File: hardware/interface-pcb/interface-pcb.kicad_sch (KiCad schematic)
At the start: 0 parts

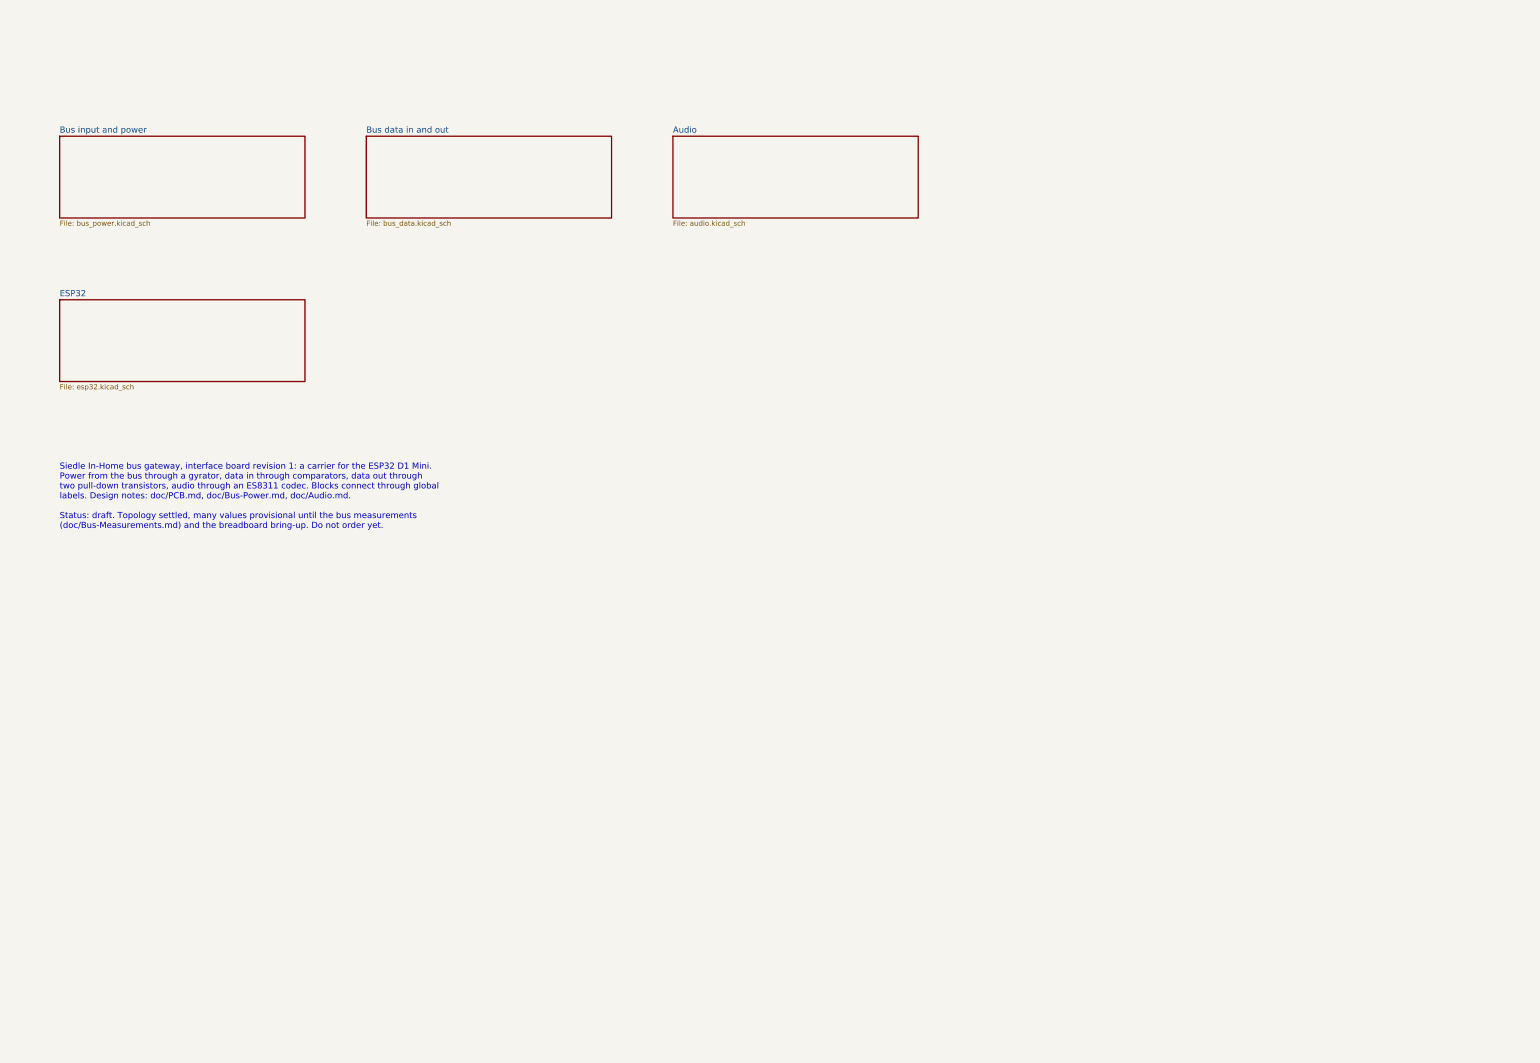
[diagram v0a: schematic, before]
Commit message: Redraw the schematic with wires
The generated draft connected everything through net labels. The redraw
wires each block so the signal paths, dividers, filters and feedback
loops can be read at a glance, with a note per block on what to measure
there. The ESP32 moves onto the root sheet, next to a map of the circuit
sheets and their test points.

The connectivity is unchanged: the exported netlist has the same 101
parts with the same values, footprints, LCSC numbers and population, and
the same pins on all 75 nets. PCB.md describes the new layout of the
sheets and what to probe where, and flags two checks for the bring-up:
the DAC still reaches the current sink while TX_EN is low, and the
comparator input range.

PDF exports go to output/, which git ignores.

Co-Authored-By: Claude Opus 5.5 <noreply@anthropic.com>
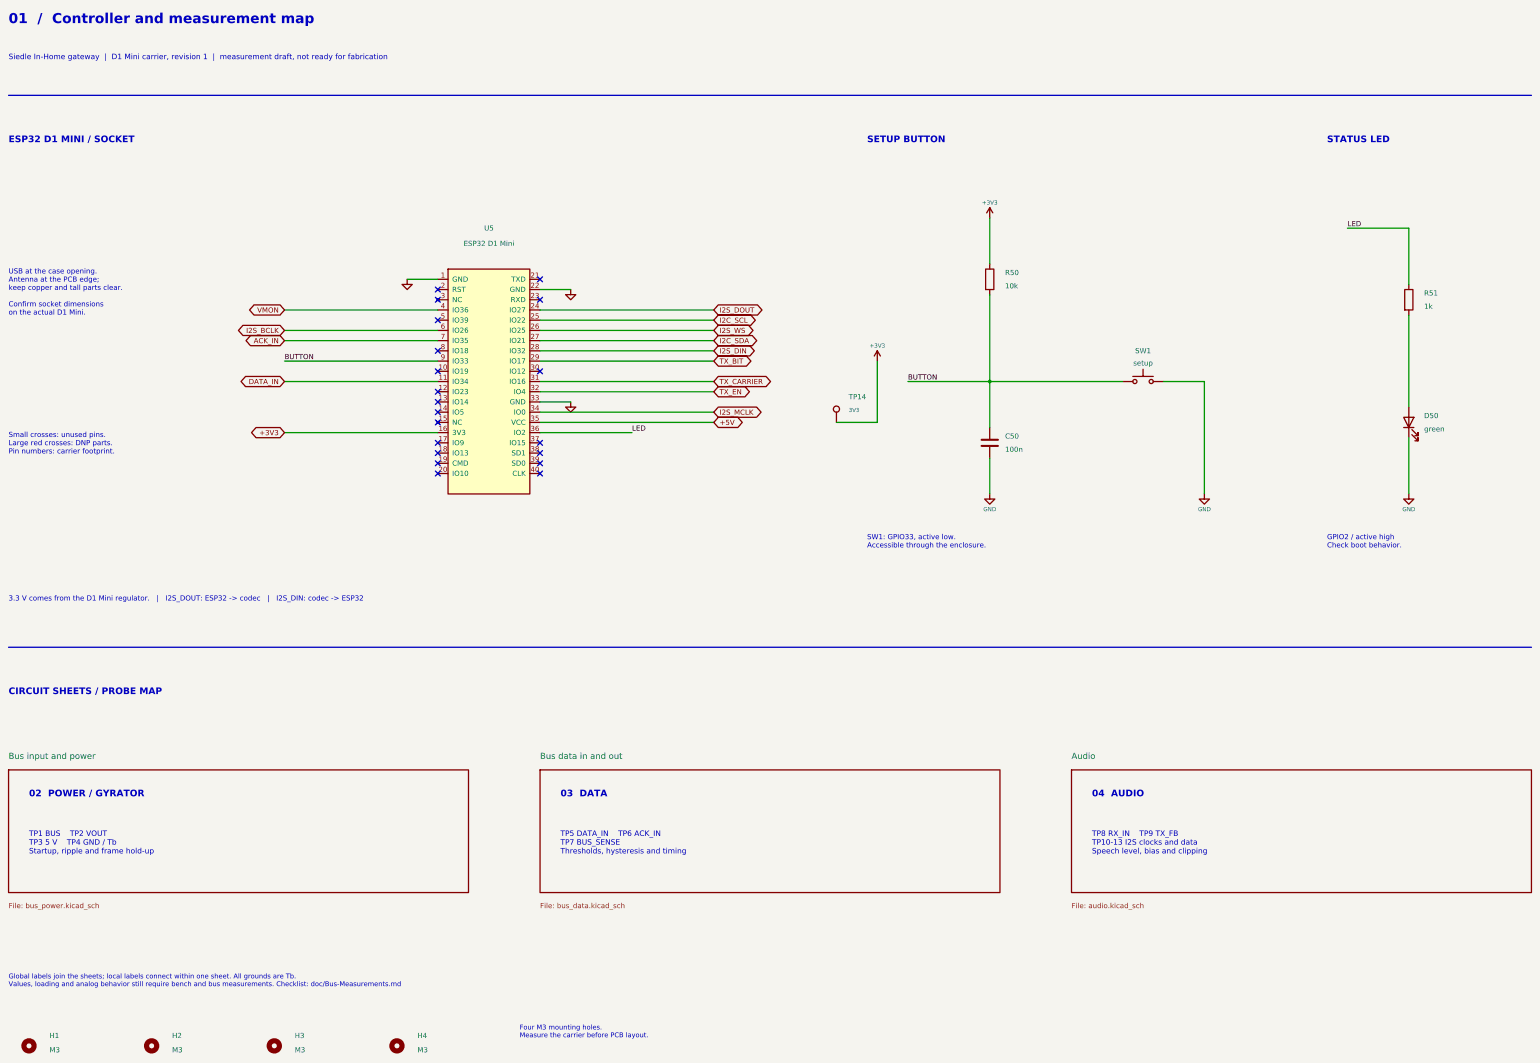
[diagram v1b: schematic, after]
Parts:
- added C50: 100n, Capacitor_SMD:C_0805_2012Metric, symbol Device:C
- added D50: green, LED_SMD:LED_0805_2012Metric, symbol Device:LED
- added H1, H2, H3, H4: M3, MountingHole:MountingHole_3.2mm_M3, symbol Mechanical:MountingHole
- added R50: 10k, Resistor_SMD:R_0805_2012Metric, symbol Device:R
- added R51: 1k, Resistor_SMD:R_0805_2012Metric, symbol Device:R
- added SW1: setup, Button_Switch_SMD:SW_Push_1P1T_XKB_TS-1187A, symbol Switch:SW_Push
- added TP14: 3V3, TestPoint:TestPoint_Pad_D1.5mm, symbol Connector:TestPoint
- added U5: ESP32 D1 Mini, gateway:D1_Mini_ESP32_Socket, symbol gateway:D1_Mini_ESP32
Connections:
- new net: D50.2 (A), R51.2
- new net +3V3: R50.1, TP14.1, U5.16 (3V3)
- new net +5V: U5.35 (VCC)
- new net ACK_IN: U5.7 (IO35)
- new net BUTTON: C50.1, R50.2, SW1.1, U5.9 (IO33)
- new net DATA_IN: U5.11 (IO34)
- new net GND: C50.2, D50.1 (K), SW1.2, U5.1 (GND), U5.22 (GND), U5.33 (GND)
- new net I2C_SCL: U5.25 (IO22)
- new net I2C_SDA: U5.27 (IO21)
- new net I2S_BCLK: U5.6 (IO26)
- new net I2S_DIN: U5.28 (IO32)
- new net I2S_DOUT: U5.24 (IO27)
- new net I2S_MCLK: U5.34 (IO0)
- new net I2S_WS: U5.26 (IO25)
- new net LED: R51.1, U5.36 (IO2)
- new net TX_BIT: U5.29 (IO17)
- new net TX_CARRIER: U5.31 (IO16)
- new net TX_EN: U5.32 (IO4)
- new net VMON: U5.4 (IO36)
- no-connect marks 0 -> 20
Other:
- removed sheet ESP32
- note added: "01 / Controller and measurement map"
- note added: "02 POWER / GYRATOR"
- note added: "03 DATA"
- note added: "04 AUDIO"
- note added: "3.3 V comes from the D1 Mini regulator. | I2S_DOUT: ESP32 -> codec | I2S_DIN: codec -> ESP32"
- note added: "CIRCUIT SHEETS / PROBE MAP"
- note added: "ESP32 D1 MINI / SOCKET"
- note added: "Four M3 mounting holes. Measure the carrier before PCB layout."
- note added: "GPIO2 / active high Check boot behavior."
- note added: "Global labels join the sheets; local labels connect within one sheet. All grounds are Tb. Values, loading and analog behavior still require bench and bus measurements. Checklist: doc/Bus-Measurements.md"
- note added: "SETUP BUTTON"
- note added: "STATUS LED"
- note added: "SW1: GPIO33, active low. Accessible through the enclosure."
- note added: "Siedle In-Home gateway | D1 Mini carrier, revision 1 | measurement draft, not ready for fabrication"
- note added: "Small crosses: unused pins. Large red crosses: DNP parts. Pin numbers: carrier footprint."
- note added: "TP1 BUS TP2 VOUT TP3 5 V TP4 GND / Tb Startup, ripple and frame hold-up"
- note added: "TP5 DATA_IN TP6 ACK_IN TP7 BUS_SENSE Thresholds, hysteresis and timing"
- note added: "TP8 RX_IN TP9 TX_FB TP10-13 I2S clocks and data Speech level, bias and clipping"
- note added: "USB at the case opening. Antenna at the PCB edge; keep copper and tall parts clear. Confirm socket dimensions on the actual D1 Mini."
- note removed: "Siedle In-Home bus gateway, interface board revision 1: a carrier for the ESP32 D1 Mini. Power from the bus through a gyrator, data in through comparators, data out through two pull-down transistors, audio through an ES8311 codec. Blocks connect through global labels. Design notes: doc/PCB.md, doc/Bus-Power.md, doc/Audio.md. Status: draft. Topology settled, many values provisional until the bus m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"
- title: Siedle gateway interface board -> 01  /  Controller and measurement map
